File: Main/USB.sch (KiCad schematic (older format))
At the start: 9 parts, among them Q1 S8050, Q2 S8050, U6 USB-A-PLUG, U7 CH340G, X1 12MHz

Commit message: initial version of v3.0
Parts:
- C1, C2: footprint (none) -> Capacitors_SMD:C_0805
- Q1, Q2: footprint TO-92 -> TO_SOT_Packages_SMD:SOT-23
- R10, R11: footprint (none) -> Resistors_SMD:R_0603
- U6: footprint (none) -> Connect:USB_Micro-B
- U7: footprint (none) -> SMD_Packages:SO-16-N
- X1: footprint (none) -> Crystals:crystal_FA238-TSX3225
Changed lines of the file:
@@
 EESchema Schematic File Version 2
-LIBS:Mirobot-rescue
 LIBS:power
 LIBS:device
@@
 LIBS:memory
 LIBS:xilinx
-LIBS:microcontrollers
-LIBS:dsp
-LIBS:microchip
-LIBS:analog_switches
-LIBS:motorola
-LIBS:texas
-LIBS:intel
-LIBS:audio
-LIBS:interface
-LIBS:digital-audio
-LIBS:philips
-LIBS:display
-LIBS:cypress
-LIBS:siliconi
-LIBS:opto
-LIBS:atmel
-LIBS:contrib
-LIBS:valves
 LIBS:mirobot
 LIBS:Mirobot-cache
@@
 F 0 "U7" H 5050 4550 60  0000 C CNN
 F 1 "CH340G" H 5025 3600 60  0000 C CNN
-F 2 "" H 5125 3875 60  0000 C CNN
+F 2 "SMD_Packages:SO-16-N" H 5125 3875 60  0001 C CNN
 F 3 "" H 5125 3875 60  0000 C CNN
 	1    5025 4075
@@
 F 0 "U6" H 4350 2700 60  0000 C CNN
 F 1 "USB-A-PLUG" H 3875 3075 60  0000 C CNN
-F 2 "" H 3925 2325 60  0000 C CNN
+F 2 "Connect:USB_Micro-B" H 3925 2325 60  0001 C CNN
 F 3 "" H 3925 2325 60  0000 C CNN
 	1    3925 2850
@@
 $EndComp
 $Comp
-L +3V3 #PWR20
+L +3V3 #PWR017
 U 1 1 56A03110
 P 5025 3375
-F 0 "#PWR20" H 5025 3225 60  0001 C CNN
+F 0 "#PWR017" H 5025 3225 60  0001 C CNN
 F 1 "+3V3" H 5025 3515 60  0000 C CNN
 F 2 "" H 5025 3375 60  0000 C CNN
@@
 Connection ~ 5025 3450
 $Comp
-L VSS #PWR18
+L VSS #PWR018
 U 1 1 56A03441
 P 3325 3375
-F 0 "#PWR18" H 3325 3225 60  0001 C CNN
+F 0 "#PWR018" H 3325 3225 60  0001 C CNN
 F 1 "VSS" H 3325 3525 60  0000 C CNN
 F 2 "" H 3325 3375 60  0000 C CNN
@@
 	4525 3925 4575 3925
 $Comp
-L GND #PWR17
+L GND #PWR019
 U 1 1 56A03AD3
 P 3100 3950
-F 0 "#PWR17" H 3100 3700 60  0001 C CNN
+F 0 "#PWR019" H 3100 3700 60  0001 C CNN
 F 1 "GND" H 3100 3800 60  0000 C CNN
 F 2 "" H 3100 3950 60  0000 C CNN
@@
 F 0 "X1" H 4150 4715 50  0000 C CNN
 F 1 "12MHz" H 4180 4515 50  0000 L CNN
-F 2 "" H 4150 4625 50  0000 C CNN
+F 2 "Crystals:crystal_FA238-TSX3225" H 4150 4625 50  0001 C CNN
 F 3 "" H 4150 4625 50  0000 C CNN
 	1    4150 4625
@@
 F 0 "C2" H 4425 5050 50  0000 L CNN
 F 1 "22pF" H 4425 4850 50  0000 L CNN
-F 2 "" H 4438 4800 50  0000 C CNN
+F 2 "Capacitors_SMD:C_0805" H 4438 4800 50  0001 C CNN
 F 3 "" H 4400 4950 50  0000 C CNN
 	1    4400 4950
@@
 F 0 "C1" H 3925 5050 50  0000 L CNN
 F 1 "22pF" H 3925 4850 50  0000 L CNN
-F 2 "" H 3938 4800 50  0000 C CNN
+F 2 "Capacitors_SMD:C_0805" H 3938 4800 50  0001 C CNN
 F 3 "" H 3900 4950 50  0000 C CNN
 	1    3900 4950
@@
 	4400 5150 4400 5100
 $Comp
-L GND #PWR19
+L GND #PWR020
 U 1 1 56A044B4
 P 4150 5275
-F 0 "#PWR19" H 4150 5025 60  0001 C CNN
+F 0 "#PWR020" H 4150 5025 60  0001 C CNN
 F 1 "GND" H 4150 5125 60  0000 C CNN
 F 2 "" H 4150 5275 60  0000 C CNN
@@
 F 0 "Q1" H 7400 4000 50  0000 L CNN
 F 1 "S8050" H 7400 3925 50  0000 L CNN
-F 2 "TO-92" H 7400 3850 50  0000 L CIN
+F 2 "TO_SOT_Packages_SMD:SOT-23" H 7400 3850 50  0001 L CIN
 F 3 "" H 7200 3925 50  0000 L CNN
 	1    7200 3925
@@
 F 0 "Q2" H 7400 4725 50  0000 L CNN
 F 1 "S8050" H 7400 4650 50  0000 L CNN
-F 2 "TO-92" H 7400 4575 50  0000 L CIN
+F 2 "TO_SOT_Packages_SMD:SOT-23" H 7400 4575 50  0001 L CIN
 F 3 "" H 7200 4650 50  0000 L CNN
 	1    7200 4650
@@
 F 0 "R11" V 6630 4650 50  0000 C CNN
 F 1 "10k" V 6550 4650 50  0000 C CNN
-F 2 "" V 6480 4650 50  0000 C CNN
+F 2 "Resistors_SMD:R_0603" V 6480 4650 50  0001 C CNN
 F 3 "" H 6550 4650 50  0000 C CNN
 	1    6550 4650
@@
 F 0 "R10" V 6630 3925 50  0000 C CNN
 F 1 "10k" V 6550 3925 50  0000 C CNN
-F 2 "" V 6480 3925 50  0000 C CNN
+F 2 "Resistors_SMD:R_0603" V 6480 3925 50  0001 C CNN
 F 3 "" H 6550 3925 50  0000 C CNN
 	1    6550 3925

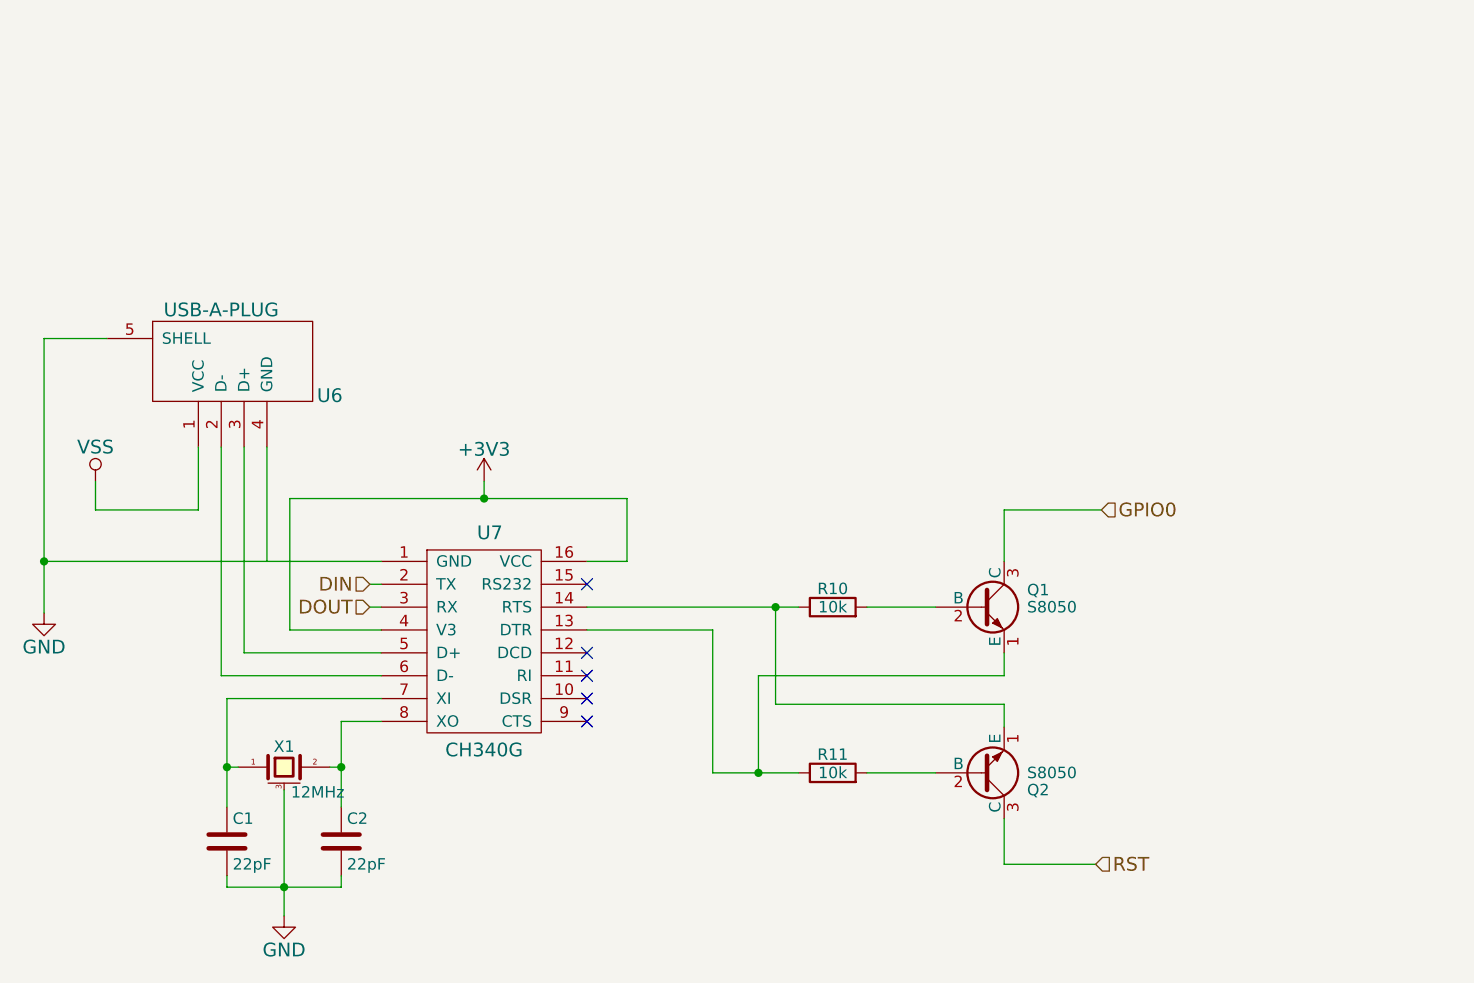
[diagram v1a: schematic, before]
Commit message: Update the BoM to embed it into KiCad
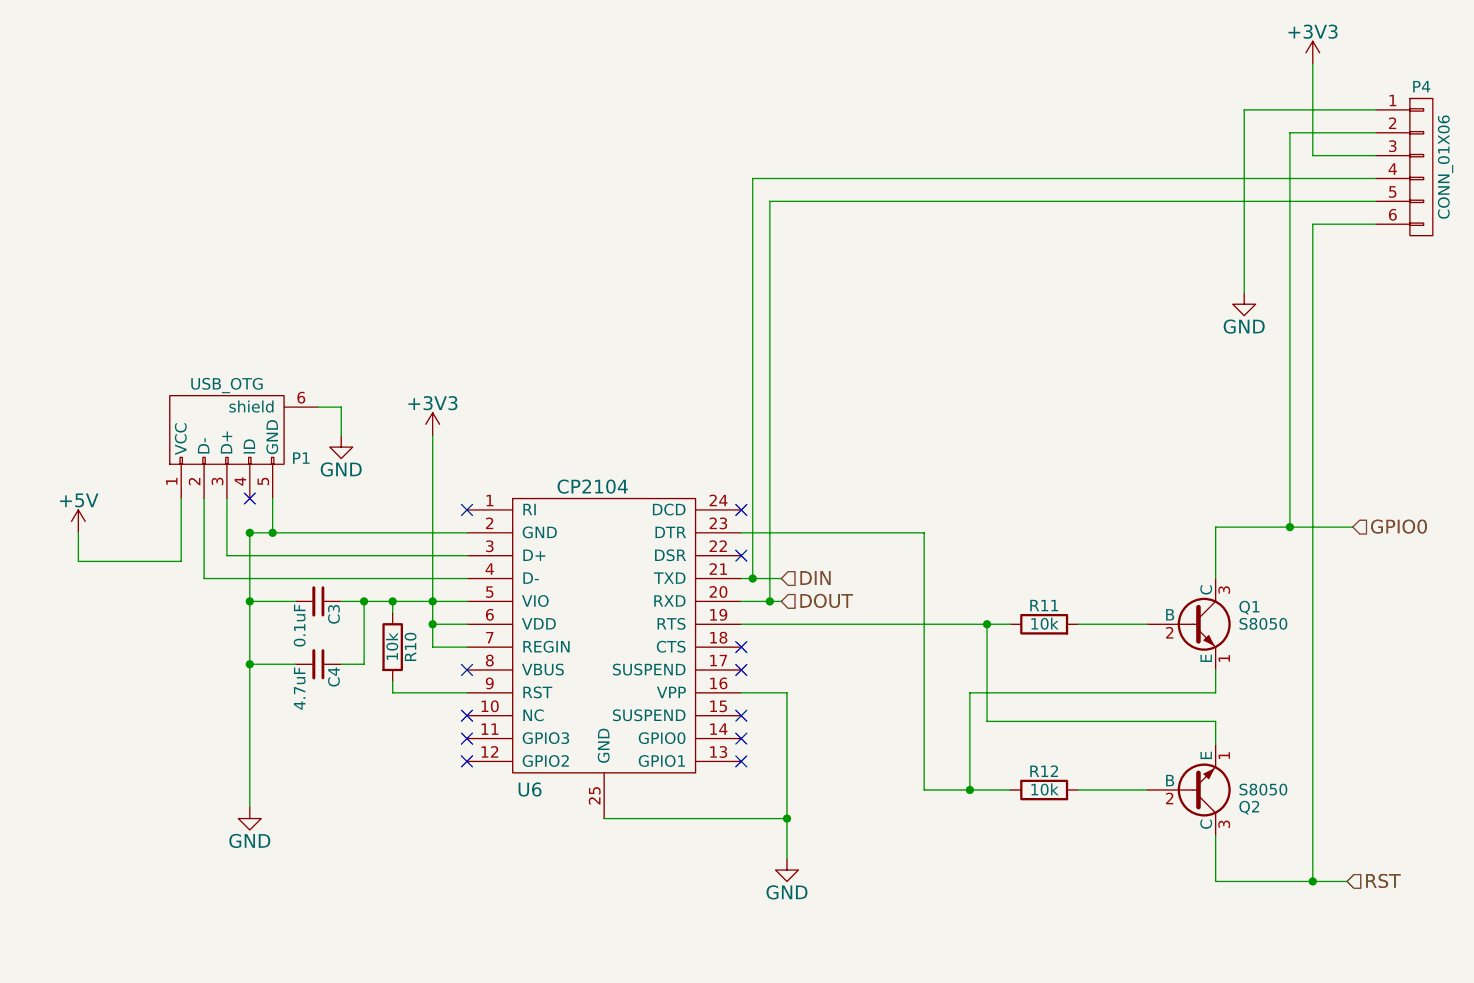
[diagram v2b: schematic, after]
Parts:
- removed C1, C2: 22pF, Capacitors_SMD:C_0805, symbol C
- removed U6: USB-A-PLUG, Connect:USB_Micro-B, symbol USB-A-PLUG
- removed U7: CH340G, SMD_Packages:SO-16-N, symbol CH340G
- removed X1: 12MHz, Crystals:crystal_FA238-TSX3225, symbol CRYSTAL_SMD
- added C3: 0.1uF, Capacitors_SMD:C_0603, symbol C_Small
- added C4: 4.7uF, Capacitors_SMD:C_0603, symbol C_Small
- added P1: USB_OTG, Custom:MOLEX_MICRO_USB, symbol USB_OTG
- added P4: CONN_01X06, Pin_Headers:Pin_Header_Straight_1x06, symbol CONN_01X06
- added R10: 10k, Resistors_SMD:R_0603, symbol R
- added U2: CP2104, Custom:QFN-24-1EP_4x4mm_Pitch0.5mm-easySolder, symbol CP2104
- Q1, Q2: footprint TO_SOT_Packages_SMD:SOT-23 -> Custom:SOT-23; Description (none) -> S8050 NPN Transistor; Package ID (none) -> SOT-23; Required (none) -> y; Source2 (none) -> http://www.aliexpress.com/item/New-original-3000PCS-8050-S8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
- R11: renamed from R10; Description (none) -> 0603 10k Resistor; Manufacturer Name (MFN) (none) -> Generic; Package ID (none) -> 0603
- R12: renamed from R11; Description (none) -> 0603 10k Resistor; Manufacturer Name (MFN) (none) -> Generic; Package ID (none) -> 0603
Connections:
- net +3V3: now also C3.1, C4.1, P4.3 (P3), R10.1, U2.5 (VIO), U2.6 (VDD), U2.7 (REGIN)
- net DIN: now also P4.4 (P4), U2.21 (TXD)
- net DOUT: now also P4.5 (P5), U2.20 (RXD)
- net GND: now also C3.2, C4.2, P1.5 (GND), P1.6 (shield), P4.1 (P1), U2.16 (VPP), U2.2 (GND), U2.25 (GND)
- net GPIO0: now also P4.2 (P2)
- net RST: now also P4.6 (P6)
- net at Q1.1 (E), R12.1: now also U2.23 (DTR)
- net at Q2.1 (E), R11.1: now also U2.19 (RTS)
- new net: P1.3 (D+), U2.3 (D+)
- new net: P1.2 (D-), U2.4 (D-)
- new net: R10.2, U2.9 (RST)
- new net +5V: P1.1 (VCC)
- no-connect marks 5 -> 13
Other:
- moved on the sheet: Q1, Q2, R11, R12
